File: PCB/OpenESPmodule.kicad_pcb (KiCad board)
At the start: 2 copper layers, 33 x 39.5 mm, 23 parts, among them J1 PINHD_1x15_Female, J3 USB_C_Receptacle_USB2.0_16P, SW1 SW_Push, SW2 SW_Push, U1 ESP32-C3-WROOM-02, U2 SPX3819M5-L-3-3, U3 MCP9700Ax-HLT, U4 4N28

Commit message: tri
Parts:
- added BT1: Battery_Cell, Battery:BatteryHolder_Keystone_1060_1x2032, B.Cu at (136.5, 94.5)
- added U5: XL1509-3.3, Package_SO:SOIC-8_3.9x4.9mm_P1.27mm, B.Cu at (153.0, 87.5)
- moved SW1 1.80 mm to (131.5, 107.2)
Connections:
- J1 pad 10: unconnected-(J1-Pad10) -> /optocoupler in
- J1 pad 9: unconnected-(J1-Pad9) -> /optocoupleur_in_gnd
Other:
- board size 33 x 39.5 mm -> 34 x 39.5 mm

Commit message: ammelioration de la carte + Update README
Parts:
- added D2: D, Diode_SMD:D_0603_1608Metric, F.Cu at (147.0, 103.3)
- D1: value LED -> IR26-21C_L110_TR8; footprint LED_THT:LED_VCCLite_5381H5_6.35x6.35mm -> LED_SMD:LED_1206_3216Metric_Pad1.42x1.75mm_HandSolder
- U5: value XL1509-3.3 -> ST1S12XX; footprint Package_SO:SOIC-8_3.9x4.9mm_P1.27mm -> Package_TO_SOT_SMD:TSOT-23-5
- moved U5 2.24 mm to (151.0, 88.5)
- moved D1 2.02 mm to (137.0, 98.0), turned to 180 degrees
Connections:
- BT1 pad 1: unconnected-(BT1-+-Pad1) -> Net-(BT1-+)
- BT1 pad 2: unconnected-(BT1---Pad2) -> Earth
- U5 pad 5: Net-(U5-GND-Pad5) -> unconnected-(U5-FB/V_{O}-Pad5)
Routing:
- net Net-(BT1-+): track 0.00 -> 5.66 mm
- net +3.3V: track 105.2 -> 109.2 mm
- net Earth: track 35.8 -> 38.4 mm
- net Net-(U2-BP): track 0.00 -> 2.18 mm
- net Net-(U1-IO9): track 28.9 -> 30.7 mm
- net +5V: track 37.4 -> 39.1 mm
- net Net-(U1-IO4): track 28.8 -> 30.1 mm
- net /Esp32_EN: track 41.1 -> 42.3 mm

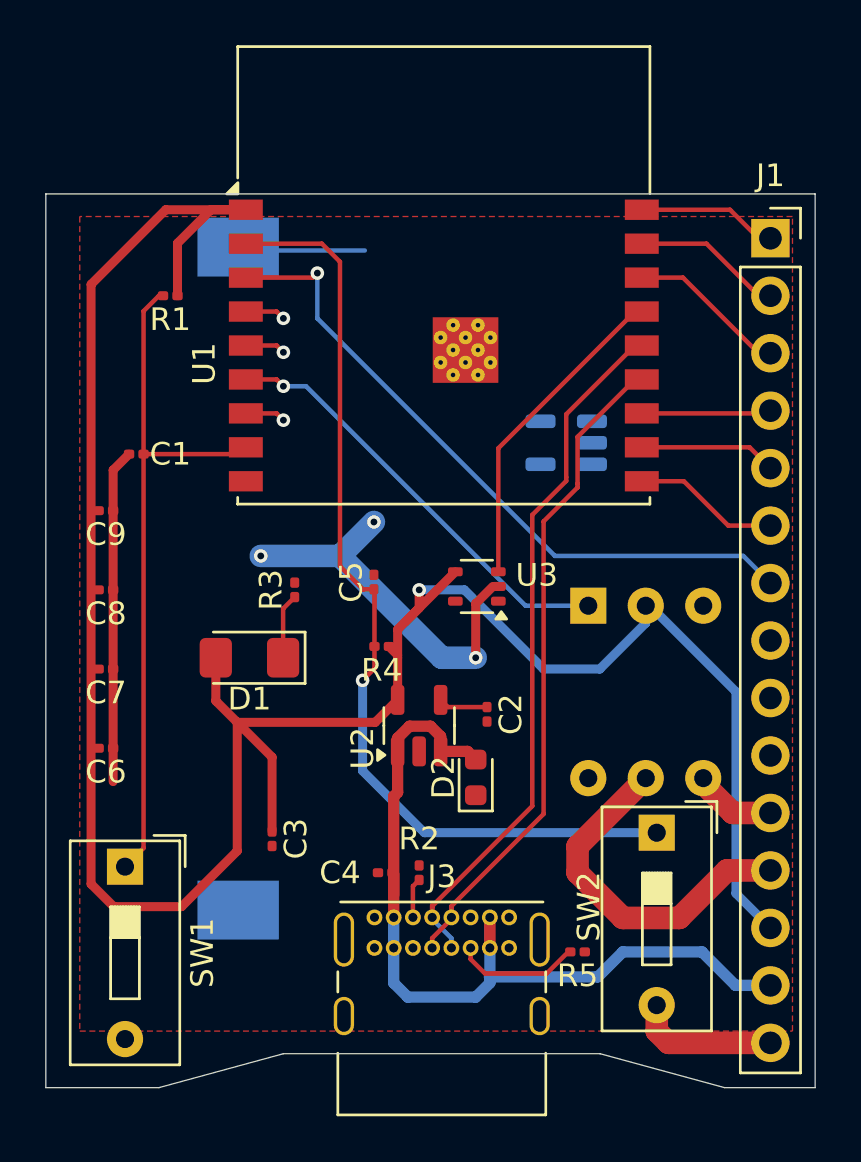
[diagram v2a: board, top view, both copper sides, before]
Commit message: Add power managment
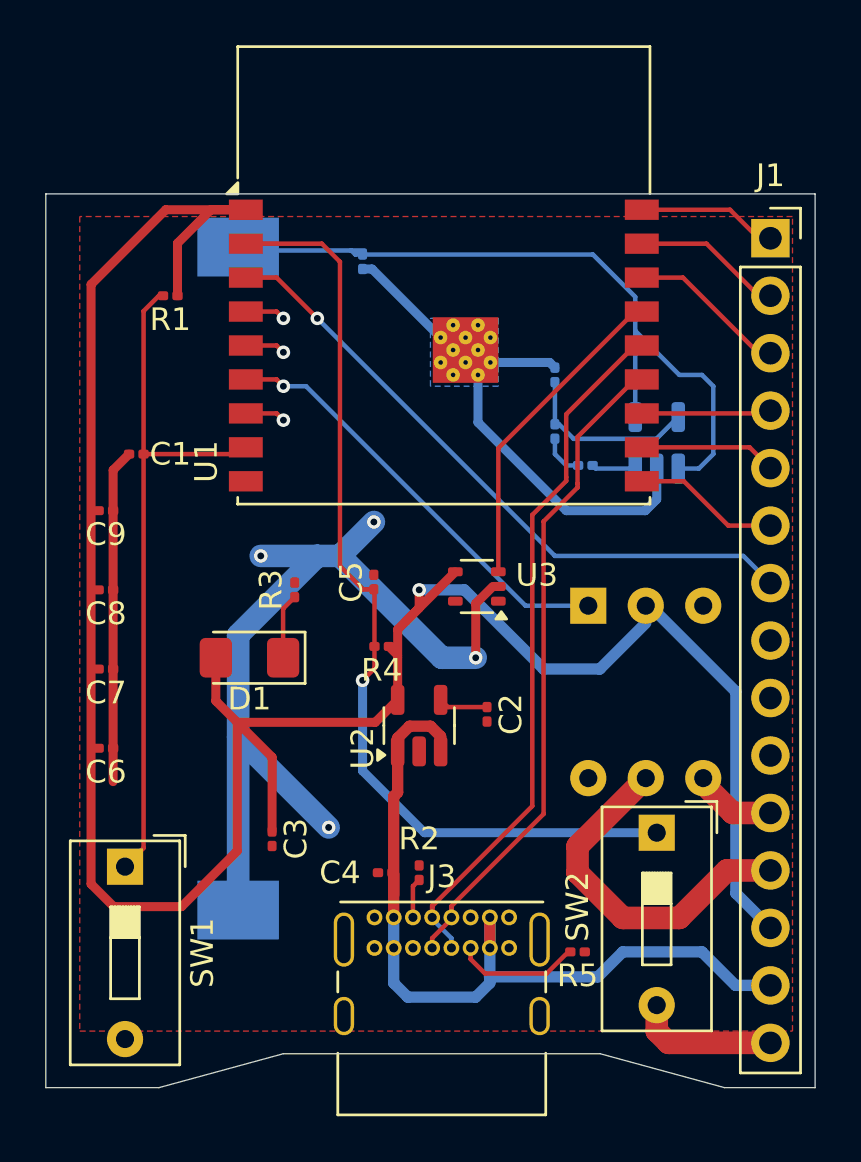
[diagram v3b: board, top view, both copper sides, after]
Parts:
- removed D2: D, Diode_SMD:D_0603_1608Metric
- removed U5: ST1S12XX, Package_TO_SOT_SMD:TSOT-23-5
- added C10: 4.7u, Capacitor_SMD:C_0201_0603Metric, B.Cu at (142.0, 80.5)
- added L1: 2.2u, Inductor_SMD:L_0201_0603Metric, B.Cu at (151.8, 89.5)
- added R6: 100k, Resistor_SMD:R_0201_0603Metric, B.Cu at (150.5, 85.5)
- added R7: 100k, Resistor_SMD:R_0201_0603Metric, B.Cu at (150.5, 88.0)
- added U6: ST1S12XX, Package_TO_SOT_SMD:TSOT-23-5, B.Cu at (155.0, 88.5)
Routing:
- net Earth: track 38.4 -> 82.8 mm, vias 3 -> 4
- net Net-(BT1-+): track 5.66 -> 33.7 mm
- net Net-(U6-FB/V_{O}): track 0.00 -> 7.98 mm
- net Net-(U6-SW): track 0.00 -> 2.10 mm
- net Net-(C11-Pad1): track 0.00 -> 1.91 mm
- net +5V: track 39.1 -> 37.4 mm
- net Net-(U1-IO4): track 30.1 -> 28.8 mm
- added copper zone on B.Cu, net Earth
